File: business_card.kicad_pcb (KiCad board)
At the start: 2 copper layers, 11 parts, among them Q1 2N3904, U1 TLC555IP

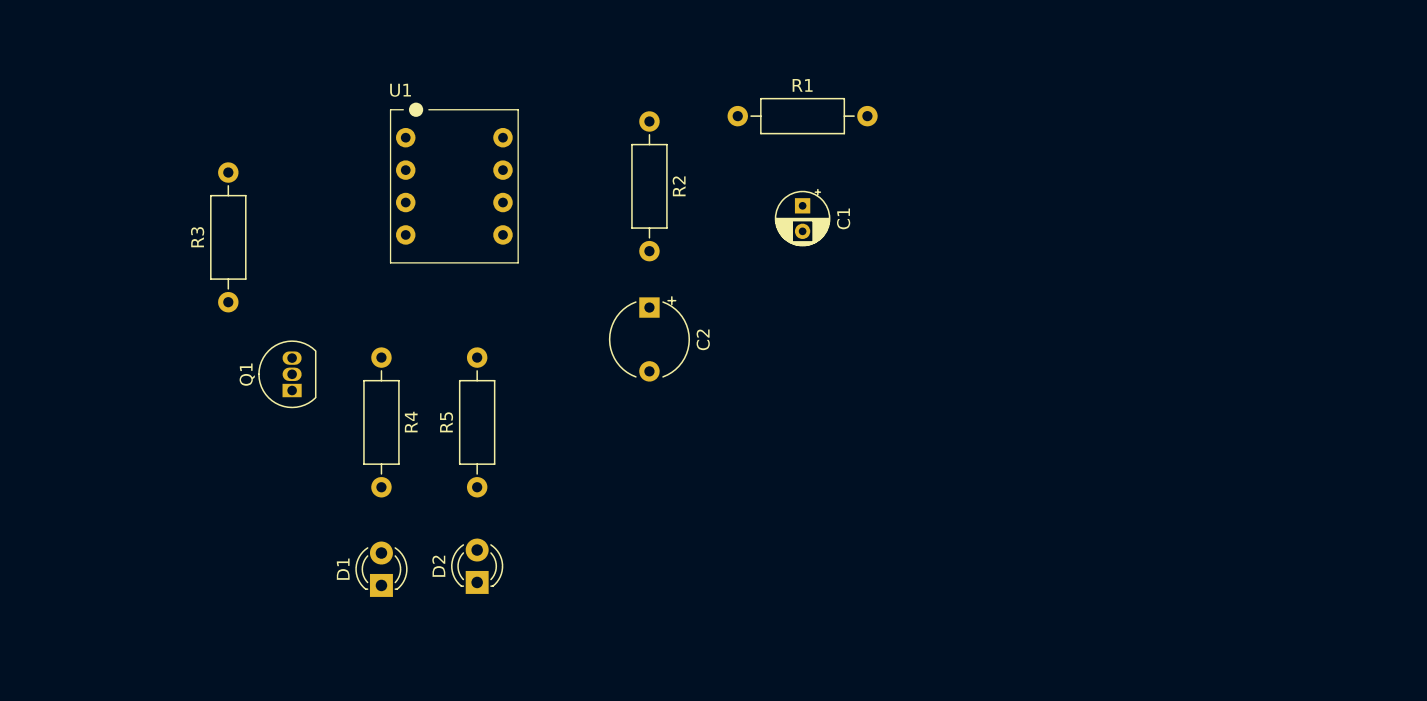
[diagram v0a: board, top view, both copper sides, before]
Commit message: Add battery holder schematic, footprint and 3d model
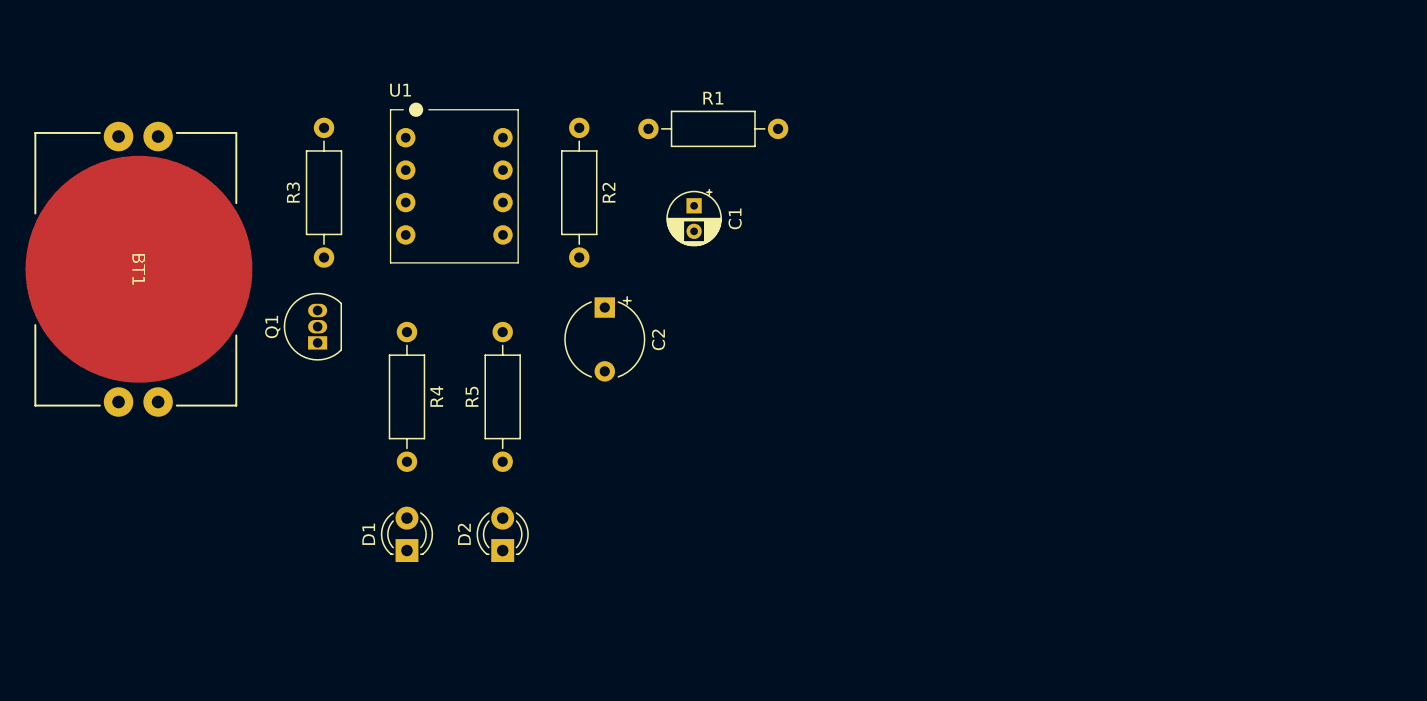
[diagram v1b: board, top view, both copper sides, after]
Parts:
- added BT1: BAT-HLD-001-THM, business_card:BAT-HLD-001-THM, F.Cu at (98.0, 98.0)
- moved C1 8.50 mm to (141.5, 93.0)
- moved R3 8.28 mm to (112.5, 97.1)
- moved R1 7.07 mm to (137.9, 87.0)
- moved R2 5.52 mm to (132.5, 86.9)
- moved Q1 4.23 mm to (112.0, 103.8)
- moved C2 3.50 mm to (134.5, 101.0)
- moved D1 3.39 mm to (119.0, 120.0)
- moved D2 3.20 mm to (126.5, 120.0)
- moved R4 2.83 mm to (119.0, 102.9)
- moved R5 2.83 mm to (126.5, 113.1)

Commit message: Add SPST switch
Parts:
- added SW1: DS01-254-S-01BE, business_card:DS01254S01BE, F.Cu at (97.5, 115.0)
- moved R2 7.00 mm to (132.5, 79.9)
- moved R3 6.00 mm to (112.5, 91.1)
- moved Q1 5.00 mm to (112.0, 98.8)
- moved U1 2.01 mm to (122.5, 93.5)

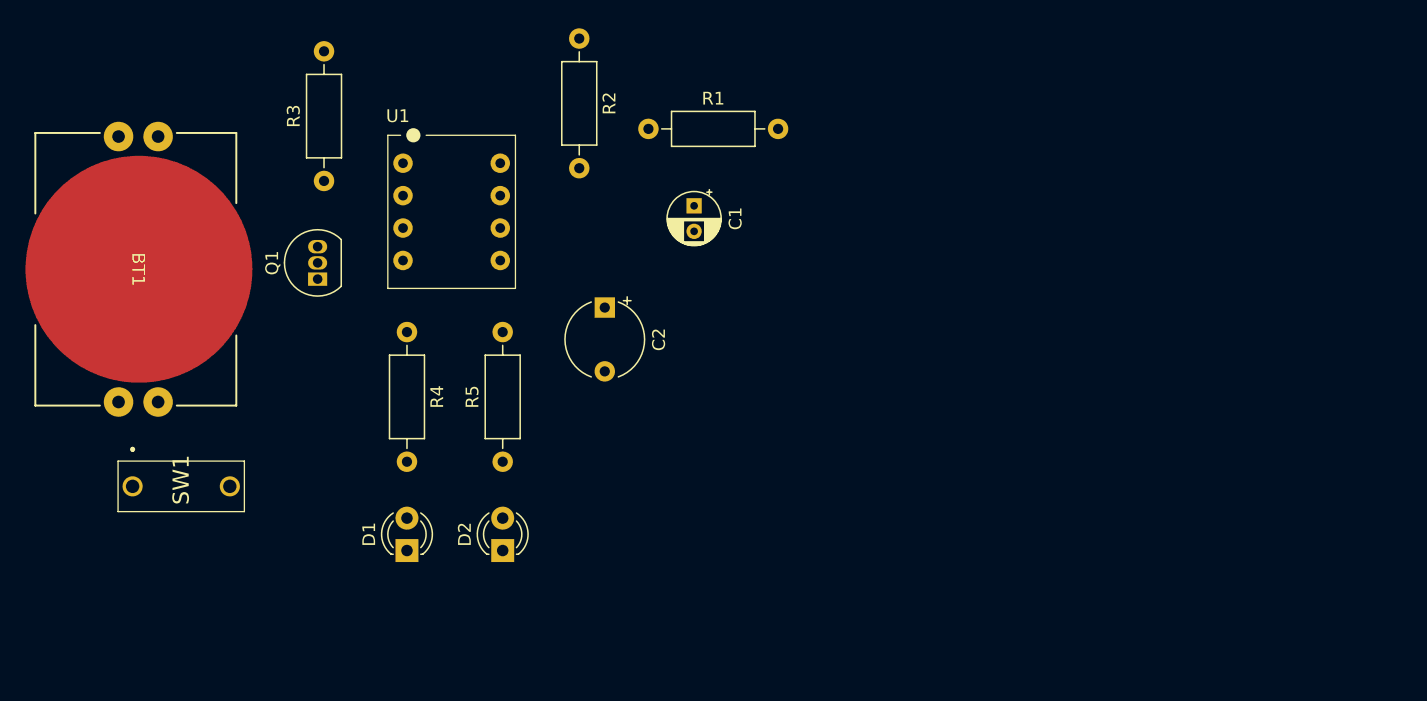
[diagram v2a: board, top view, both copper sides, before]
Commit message: Add potentiometer and update switch footprint
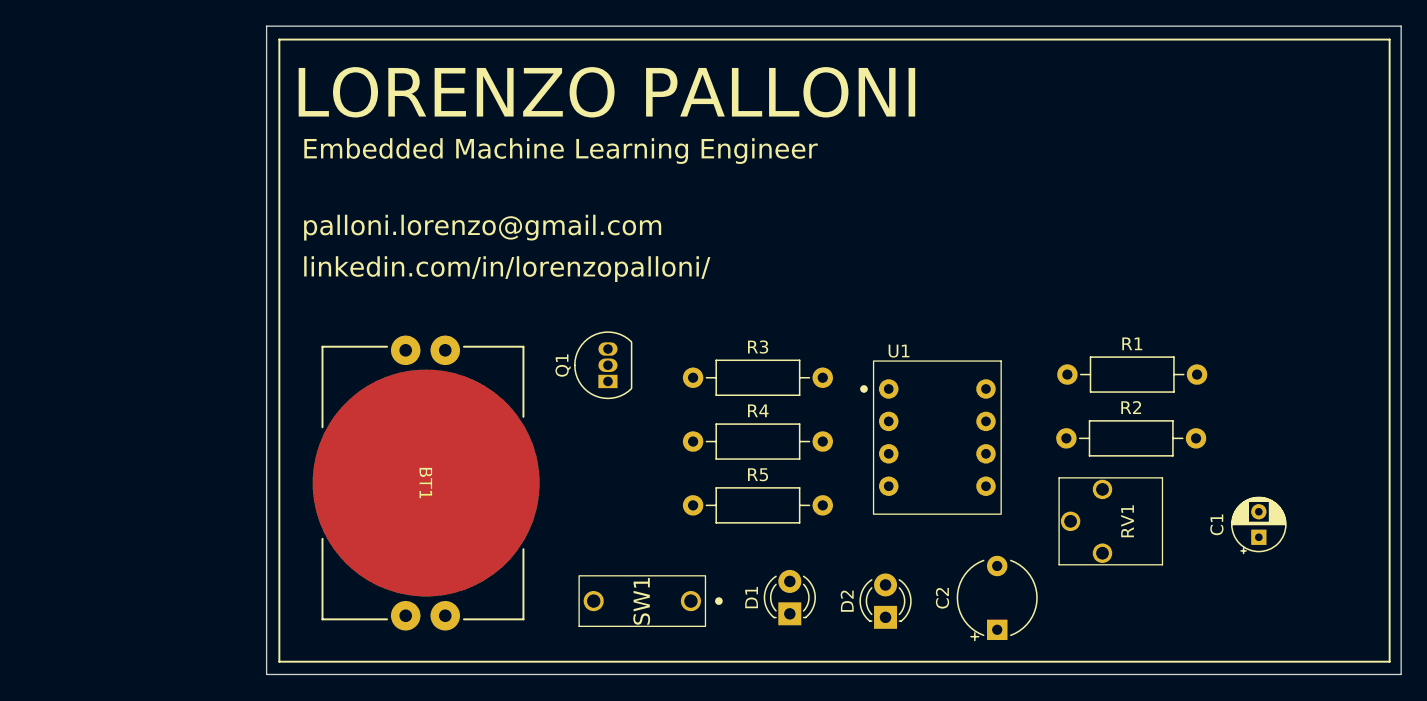
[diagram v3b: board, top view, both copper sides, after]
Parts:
- added RV1: 500K, business_card:3306P-1-504, F.Cu at (173.5, 117.8)
- R2: value 100K -> 10K
- SW1: footprint business_card:DS01254S01BE -> business_card:DS01-254-S-01BE
- moved C1 51.3 mm to (185.8, 119.0), turned to 90 degrees
- moved R2 49.4 mm to (170.7, 111.2), turned to 0 degrees
- moved U1 42.0 mm to (160.6, 111.2)
- moved SW1 40.9 mm to (137.4, 124.0), turned to 90 degrees
- moved C2 39.8 mm to (165.2, 126.2), turned to 90 degrees
- moved R1 38.1 mm to (170.8, 106.2)
- moved R3 32.8 mm to (141.4, 106.5), turned to 0 degrees
- moved D2 30.5 mm to (156.5, 125.3)
- moved D1 30.4 mm to (149.0, 125.0)
- moved BT1 28.1 mm to (120.5, 114.8)
- moved Q1 24.1 mm to (134.8, 106.8)
- moved R4 24.0 mm to (141.4, 111.5), turned to 0 degrees
- moved R5 15.3 mm to (141.4, 116.5), turned to 0 degrees
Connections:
- R2 pad 1: /DISCH -> Net-(R2-Pad1)
- R2 pad 2: /THRES/TRIG -> /DISCH
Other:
- board outline added: 88.9 x 50.8 mm
- rule pad_to_mask_clearance: 0 -> 0.1
- board text added: "Embedded Machine Learning Engineer"
- board text added: "LORENZO PALLONI"
- board text added: "linkedin.com/in/lorenzopalloni/"
- board text added: "palloni.lorenzo@gmail.com"
